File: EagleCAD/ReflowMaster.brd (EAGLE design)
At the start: 44.7 x 41.1 mm, 42 parts, among them Q1 600mA/40V, SW1 SPST_TACT-KMR2, X2 32.768

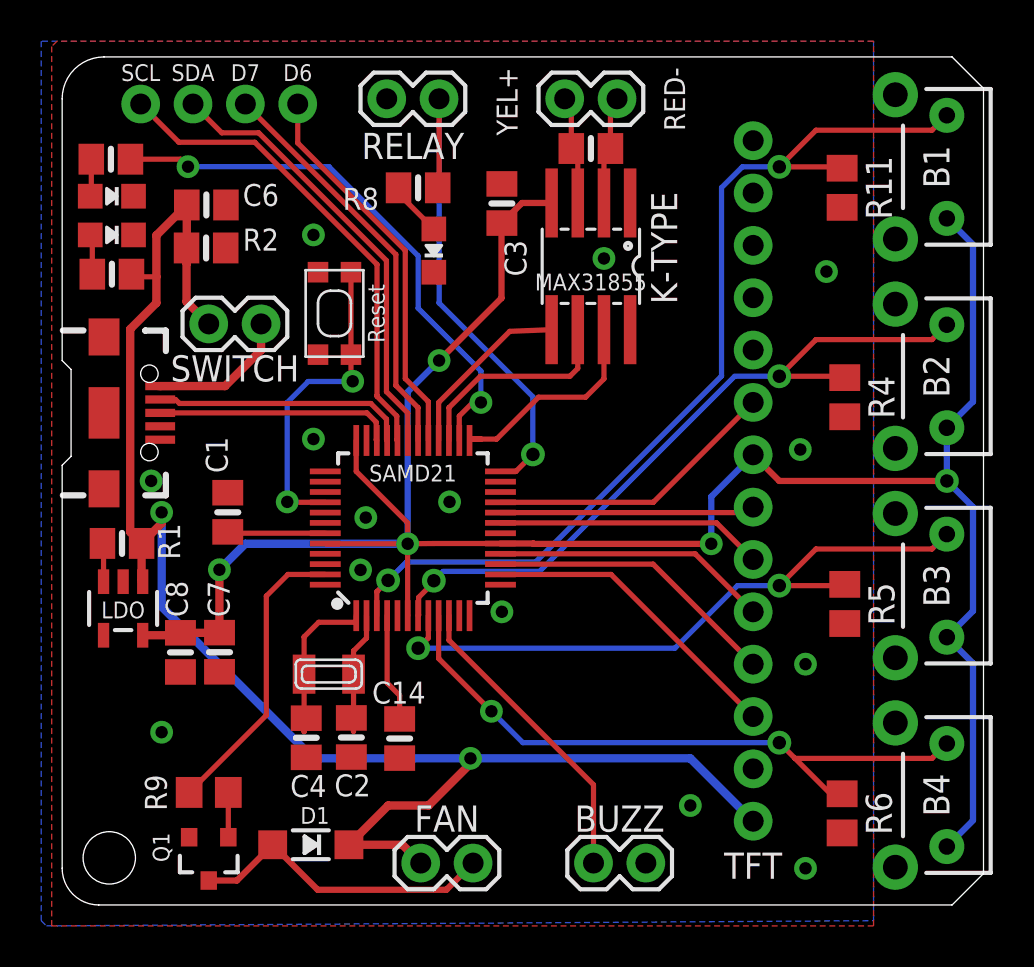
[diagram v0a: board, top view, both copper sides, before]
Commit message: added a programming header + PCB tweaks
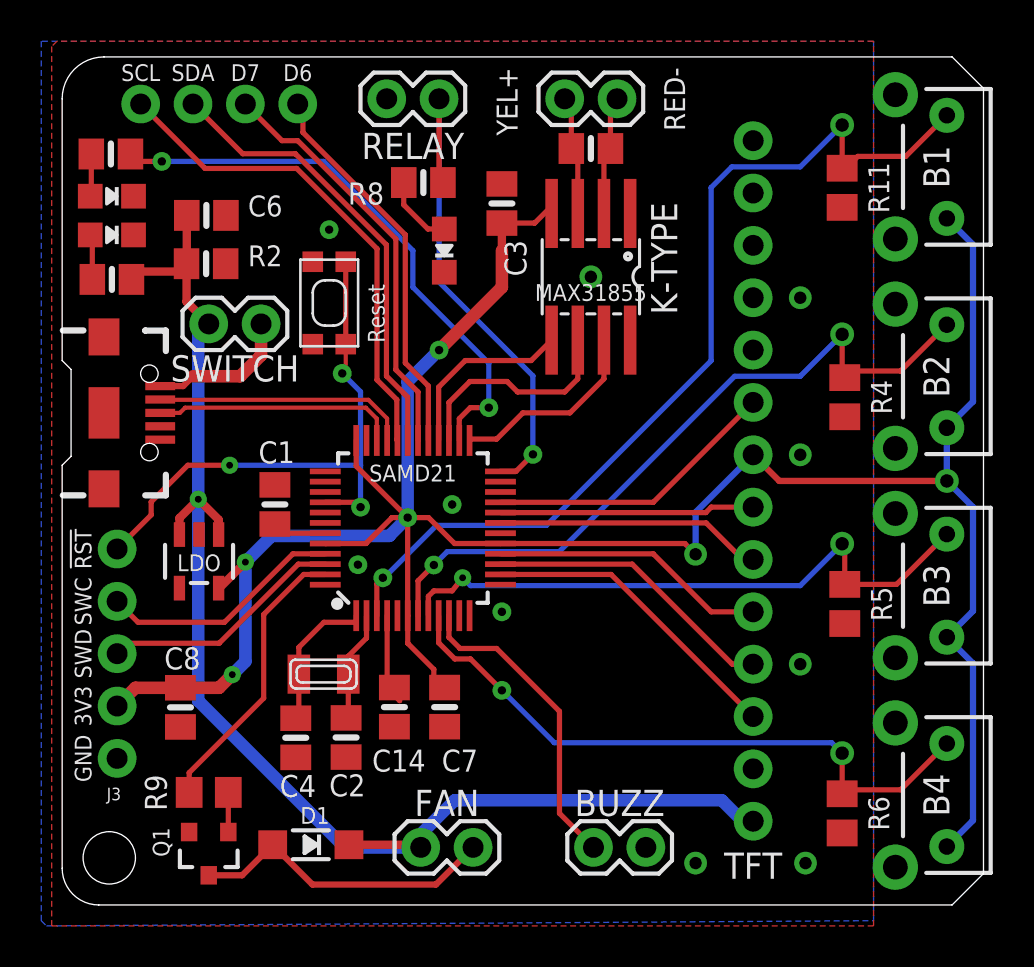
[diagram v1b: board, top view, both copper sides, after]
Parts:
- removed R1: 100k, microbuilder:0805-NO
- added J3: (no value), SparkFun-Connectors:1X05_NO_SILK
- moved C7 11.2 mm to (31.0, 11.6)
- moved LDO 4.33 mm to (19.1, 18.7)
- moved C8 2.67 mm to (18.2, 11.6)
- moved C1 2.32 mm to (22.8, 21.5)
- moved C14 1.55 mm to (28.6, 11.6)
- moved R2 0.76 mm to (19.4, 33.1)
- moved BUZZ 0.76 mm to (38.2, 4.83)
- moved FAN 0.76 mm to (29.8, 4.83)
- moved SW1 0.57 mm to (25.4, 31.2)
- moved C6 0.51 mm to (19.4, 35.5)
- moved MAX31855 0.51 mm to (38.1, 32.5)
- moved 2 0.51 mm to (31.0, 33.8)
- moved C4 0.51 mm to (23.8, 10.1)
- moved R8 0.36 mm to (30.0, 37.1)
- moved R3 0.25 mm to (14.9, 32.4)
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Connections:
- removed net EN: LDO.3, R1.2
- new net VBUS_SW: C6.1, D1.C, FAN.1, LDO.1, LDO.3, R2.1, R3.1, SWITCH.2, TFT.1
- net !RESET: now also J3.5
- net +3V3: now also J3.2
- net GND: now also J3.1
- net SWCLK: now also J3.4
- net SWDIO: now also J3.3
- net VBUS: no longer C6.1, D1.C, FAN.1, LDO.1, R1.1, R2.1, R3.1, SWITCH.2, TFT.1
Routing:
- net VBUS: track 86.8 -> 7.04 mm, vias 2 -> 0
- net VBUS_SW: track 0.00 -> 66.5 mm, vias 0 -> 1
- net !RESET: track 15.6 -> 28.0 mm, vias 2 -> 3
- net SWDIO: track 0.00 -> 11.9 mm
- net SWCLK: track 0.00 -> 11.9 mm
- net +3V3: track 114.2 -> 124.5 mm, vias 5 -> 6
- net A2: track 32.9 -> 30.4 mm
- net VDDCORE: track 4.76 -> 2.83 mm
- net EN: track 1.88 -> 0.00 mm
- net N$5: track 8.39 -> 7.10 mm
- net N$7: track 6.54 -> 5.37 mm
- net D11: track 10.6 -> 9.64 mm
- net A3: track 32.0 -> 31.1 mm
- net D13: track 26.8 -> 27.6 mm
- net N$3: track 2.71 -> 3.53 mm
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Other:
- board text added: "!RST"
- board text added: "3V3"
- board text added: "GND"
- board text added: "SWC"
- board text added: "SWD"
